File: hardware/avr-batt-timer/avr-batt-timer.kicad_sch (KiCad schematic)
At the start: 6 parts, among them Q1 RFP30N06LE, U1 ATtiny5-TS

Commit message: Added most components.
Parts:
- removed Q1: RFP30N06LE, Package_TO_SOT_THT:TO-220-3_Horizontal_TabDown, symbol Timofei_Import:RFP30N06LE
- added J1: XT60PW-M, Connector_AMASS:AMASS_XT60PW-M_1x02_P7.20mm_Horizontal, symbol Timofei_Import:XT60PW-M
- added J2: XT60PW-F, Connector_AMASS:AMASS_XT60PW-F_1x02_P7.20mm_Horizontal, symbol Timofei_Import:XT60PW-F
- added MOSFET1: IRFZ44N_127, Package_TO_SOT_THT:TO-220-2_Horizontal_TabDown, symbol Timofei_Import:IRFZ44N_127
- added R4: ~ 10K, Resistor_SMD:R_0805_2012Metric_Pad1.20x1.40mm_HandSolder, symbol Device:R
- added U2: L78L05_SOT89, Package_TO_SOT_SMD:SOT-89-3, symbol Regulator_Linear:L78L05_SOT89
- R1: value 2M2 -> 10M
- R2: value 10M -> 5M
- R3: value > 10K -> ~ 250R
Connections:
- net +3V3: no longer U1.5 (VCC)
- net GND: now also J1.1, J1.3, J1.4, J2.3 (MH1), J2.4 (MH2), MOSFET1.3 (S), R4.2, U2.2 (GND)
- net at R3.1: now also MOSFET1.1 (G), R4.1
- net TPICLK: now reaches R3.2, U1.4 (PB2)
- new net +5V: U1.5 (VCC), U2.1 (OUT)
- new net LOAD: J2.1, MOSFET1.2 (D)
- new net VDD: J1.2, J2.2, U2.3 (IN)
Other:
- note added: "ADD BACK-EMF PROTECTION DIODE!!!"
- note added: "ADD LED!!!"
- note added: "ADD TPICLK!!!!!"
- moved on the sheet: R3

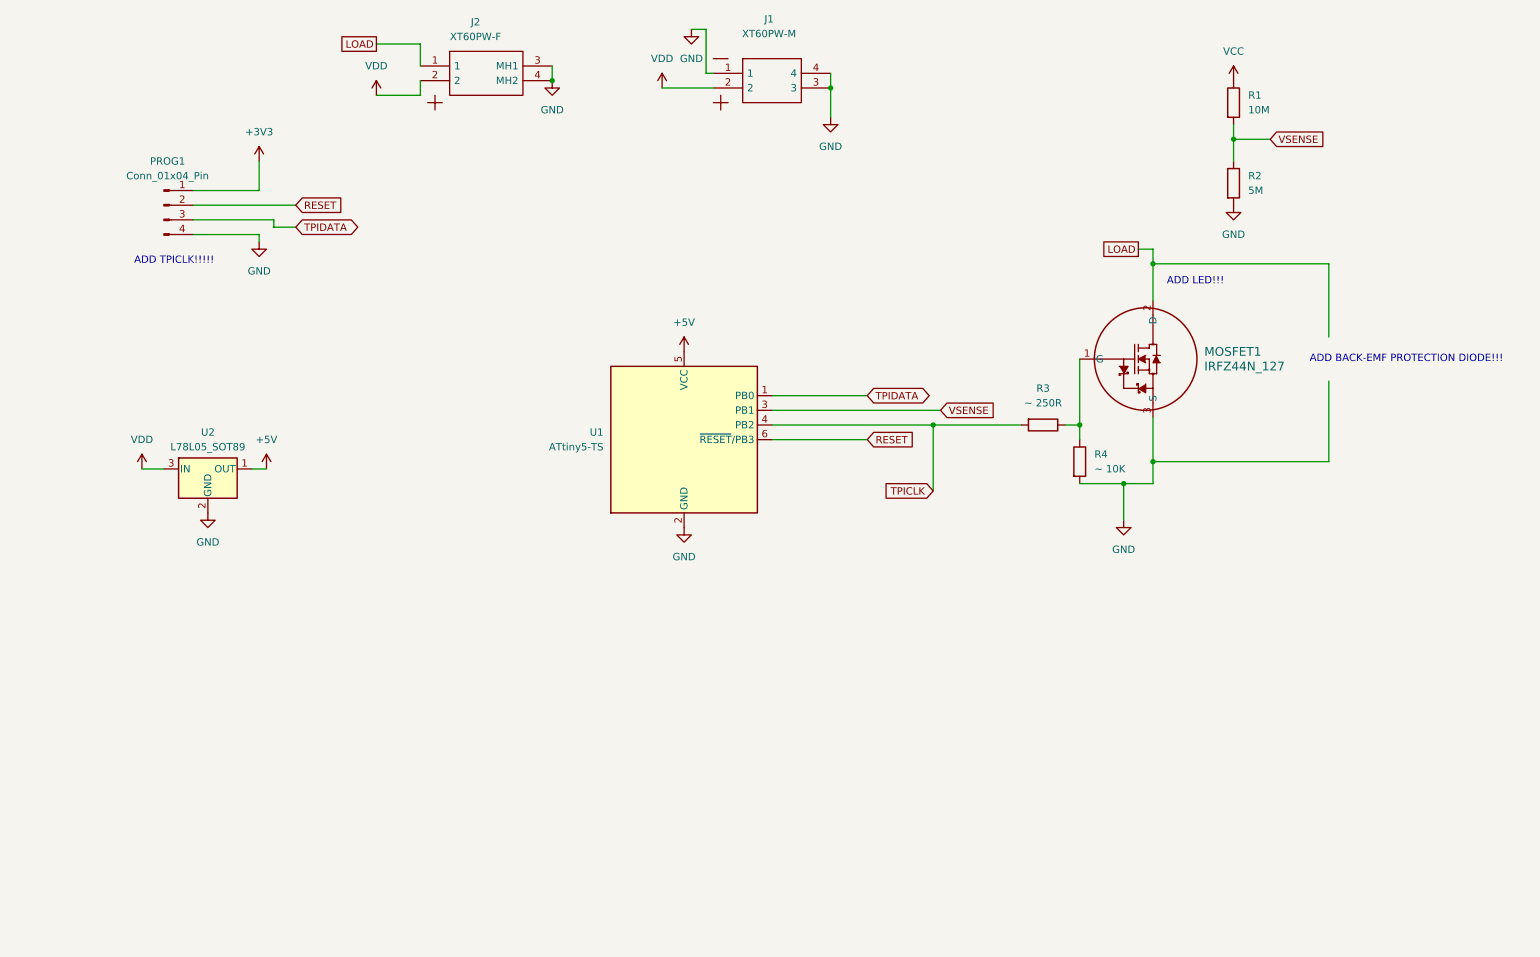
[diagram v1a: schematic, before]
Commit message: Added components. Initial PCB design.
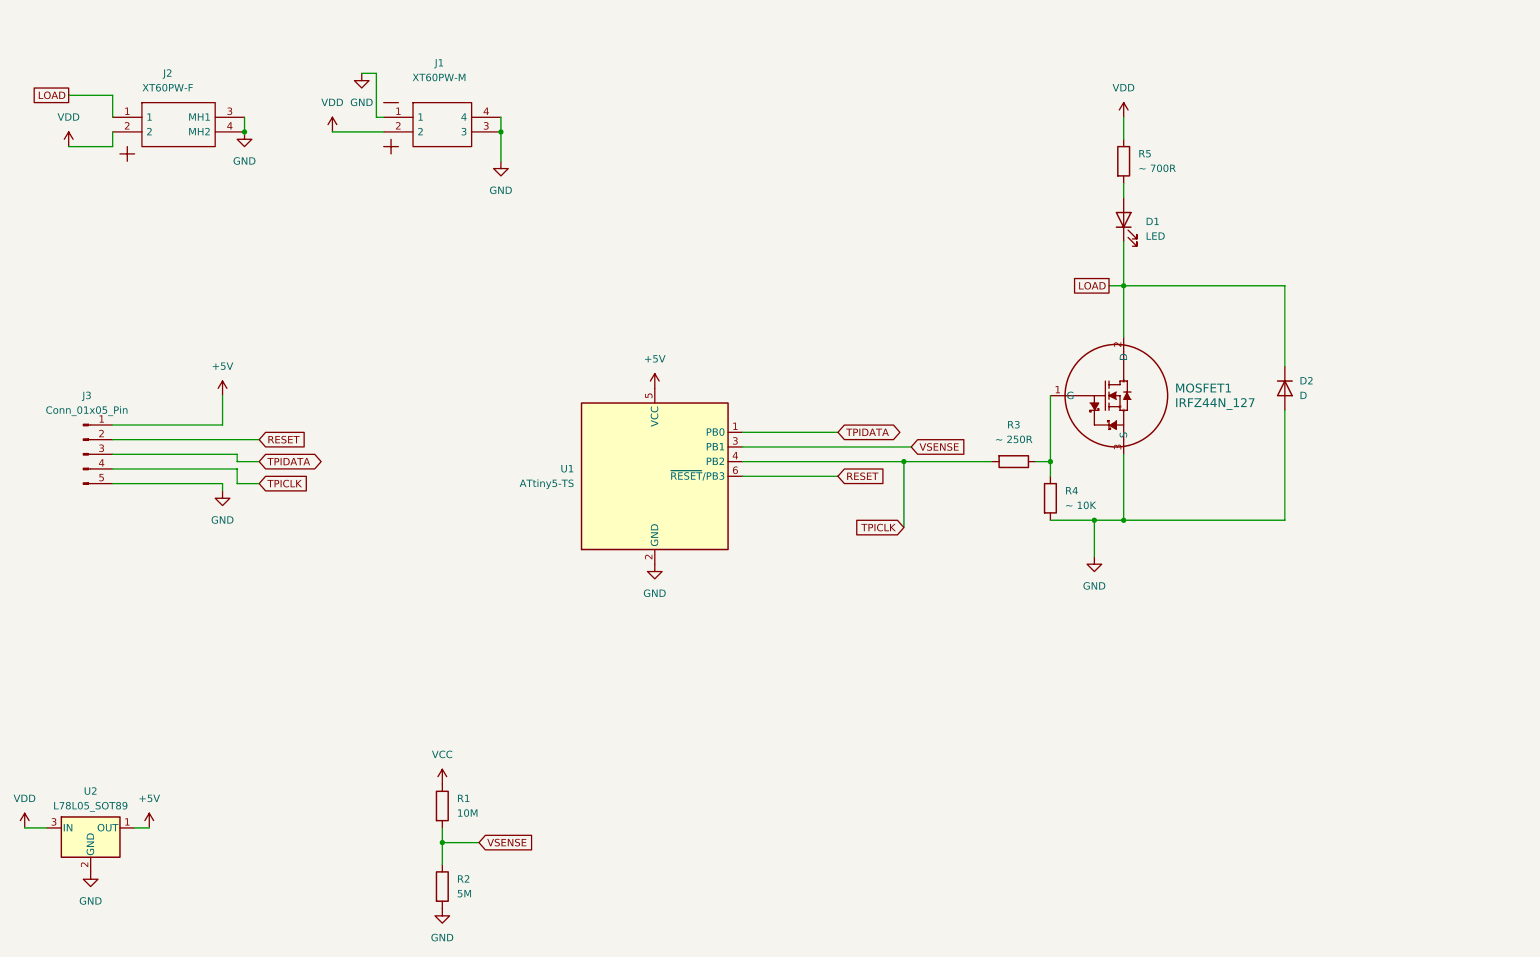
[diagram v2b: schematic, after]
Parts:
- removed PROG1: Conn_01x04_Pin, Connector_PinHeader_2.54mm:PinHeader_1x04_P2.54mm_Vertical, symbol Connector:Conn_01x04_Pin
- added D1: LED, LED_THT:LED_D3.0mm, symbol Device:LED
- added D2: D, Package_TO_SOT_THT:TO-220-2_Horizontal_TabDown, symbol Device:D
- added J3: Conn_01x05_Pin, Connector_PinHeader_2.54mm:PinHeader_1x05_P2.54mm_Vertical, symbol Connector:Conn_01x05_Pin
- added R5: ~ 700R, Resistor_SMD:R_0805_2012Metric_Pad1.20x1.40mm_HandSolder, symbol Device:R
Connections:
- net +5V: now also J3.1 (Pin_1)
- net GND: now also D2.2 (A), J3.5 (Pin_5)
- net LOAD: now also D1.1 (K), D2.1 (K)
- net RESET: now also J3.2 (Pin_2)
- net TPICLK: now also J3.4 (Pin_4)
- net TPIDATA: now also J3.3 (Pin_3)
- net VDD: now also R5.1
- new net: D1.2 (A), R5.2
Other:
- note removed: "ADD BACK-EMF PROTECTION DIODE!!!"
- note removed: "ADD LED!!!"
- note removed: "ADD TPICLK!!!!!"
- company: (none) -> Timofei Korostelev
- title: (none) -> avr-batt-timer
- moved on the sheet: J1, J2, MOSFET1, R1, R2, R3, R4, U1, U2

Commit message: +1
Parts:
- MOSFET1: footprint Package_TO_SOT_THT:TO-220-2_Horizontal_TabDown -> SOT78_TO220_NXP
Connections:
- net VCC is gone; now on net VDD: R1.1
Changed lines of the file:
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@@
+	(symbol
+		(lib_id "power:VDD")
+		(at 99.06 157.48 0)
+		(unit 1)
+		(exclude_from_sim no)
+		(in_bom yes)
+		(on_board yes)
+		(dnp no)
+		(fields_autoplaced yes)
+		(property "Reference" "#PWR06"
+			(at 99.06 161.29 0)
+			(effects
+				(font
+					(size 1.27 1.27)
+				)
+				(hide yes)
+			)
+		)
+		(property "Value" "VDD"
+			(at 99.06 152.4 0)
+			(effects
+				(font
+					(size 1.27 1.27)
+				)
+			)
+		)
+		(property "Footprint" ""
+			(at 99.06 157.48 0)
+			(effects
+				(font
+					(size 1.27 1.27)
+				)
+				(hide yes)
+			)
+		)
+		(property "Datasheet" ""
+			(at 99.06 157.48 0)
+			(effects
+				(font
+					(size 1.27 1.27)
+				)
+				(hide yes)
+			)
+		)
+		(property "Description" "Power symbol creates a global label with name \"VDD\""
+			(at 99.06 157.48 0)
+			(effects
+				(font
+					(size 1.27 1.27)
+				)
+				(hide yes)
+			)
+		)
+		(pin "1"
+		)
+		(instances
+			(project "avr-batt-timer"
+				(path "/3df09f8e-c59c-4ad6-a416-97010d9cd963"
+					(reference "#PWR06")
+					(unit 1)
+				)
+			)
+		)
+	)
 	(symbol
 		(lib_id "power:VDD")
@@
 	)
 	(symbol
-		(lib_id "power:VCC")
-		(at 99.06 157.48 0)
-		(unit 1)
-		(exclude_from_sim no)
-		(in_bom yes)
-		(on_board yes)
-		(dnp no)
-		(fields_autoplaced yes)
-		(property "Reference" "#PWR06"
-			(at 99.06 161.29 0)
-			(effects
-				(font
-					(size 1.27 1.27)
-				)
-				(hide yes)
-			)
-		)
-		(property "Value" "VCC"
-			(at 99.06 152.4 0)
-			(effects
-				(font
-					(size 1.27 1.27)
-				)
-			)
-		)
-		(property "Footprint" ""
-			(at 99.06 157.48 0)
-			(effects
-				(font
-					(size 1.27 1.27)
-				)
-				(hide yes)
-			)
-		)
-		(property "Datasheet" ""
-			(at 99.06 157.48 0)
-			(effects
-				(font
-					(size 1.27 1.27)
-				)
-				(hide yes)
-			)
-		)
-		(property "Description" "Power symbol creates a global label with name \"VCC\""
-			(at 99.06 157.48 0)
-			(effects
-				(font
-					(size 1.27 1.27)
-				)
-				(hide yes)
-			)
-		)
-		(pin "1"
-		)
-		(instances
-			(project ""
-				(path "/3df09f8e-c59c-4ad6-a416-97010d9cd963"
-					(reference "#PWR06")
-					(unit 1)
-				)
-			)
-		)
-	)
-	(symbol
 		(lib_id "MCU_Microchip_ATtiny:ATtiny5-TS")
 		(at 135.89 104.14 0)
@@
 			)
 		)
-		(property "Footprint" "Package_TO_SOT_THT:TO-220-2_Horizontal_TabDown"
+		(property "Footprint" "SOT78_TO220_NXP"
 			(at 198.12 83.058 0)
 			(effects

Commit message: +1
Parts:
- D2: value D -> D 15A
- MOSFET1: value IRFZ44N_127 -> IRFZ44N; footprint SOT78_TO220_NXP -> Package_TO_SOT_THT:TO-220-3_Horizontal_TabDown
- R3: value ~ 250R -> ~250R
- R4: value ~ 10K -> ~10K
- R5: value ~ 700R -> ~700R
- U1: value ATtiny5-TS -> ATtiny5
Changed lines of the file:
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@@
 			)
 		)
-		(property "Value" "~ 250R"
+		(property "Value" "~250R"
 			(at 198.12 97.79 90)
 			(effects
@@
 			)
 		)
-		(property "Value" "~ 700R"
+		(property "Value" "~700R"
 			(at 219.71 50.7999 0)
 			(effects
@@
 			)
 		)
-		(property "Value" "D"
+		(property "Value" "D 15A"
 			(at 247.65 90.1699 90)
 			(effects
@@
 			)
 		)
-		(property "Value" "~ 10K"
+		(property "Value" "~10K"
 			(at 207.01 109.2199 0)
 			(effects
@@
 			)
 		)
-		(property "Value" "ATtiny5-TS"
+		(property "Value" "ATtiny5"
 			(at 121.92 105.4099 0)
 			(effects
@@
 			)
 		)
-		(property "Value" "IRFZ44N_127"
+		(property "Value" "IRFZ44N"
 			(at 226.06 91.4399 0)
 			(effects
@@
 			)
 		)
-		(property "Footprint" "SOT78_TO220_NXP"
+		(property "Footprint" "Package_TO_SOT_THT:TO-220-3_Horizontal_TabDown"
 			(at 198.12 83.058 0)
 			(effects

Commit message: Fixed TPICLK pin connection. Replaced programming pins with holes.
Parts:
- removed J3: Conn_01x05_Pin, Connector_PinHeader_2.54mm:PinHeader_1x05_P2.54mm_Vertical, symbol Connector:Conn_01x05_Pin
- added TP1: +5V, TestPoint:TestPoint_Plated_Hole_D2.0mm, symbol Connector:TestPoint
- added TP2: RST, TestPoint:TestPoint_Plated_Hole_D2.0mm, symbol Connector:TestPoint
- added TP3: TDAT, TestPoint:TestPoint_Plated_Hole_D2.0mm, symbol Connector:TestPoint
- added TP4: TCLK, TestPoint:TestPoint_Plated_Hole_D2.0mm, symbol Connector:TestPoint
- added TP5: GND, TestPoint:TestPoint_Plated_Hole_D2.0mm, symbol Connector:TestPoint
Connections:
- net VSENSE is gone; now on net TPICLK: R1.2, R2.1, U1.3 (PB1)
- net +5V: now also TP1.1
- net GND: now also TP5.1
- net RESET: now also TP2.1
- net TPICLK: now also TP4.1; no longer R3.2, U1.4 (PB2)
- net TPIDATA: now also TP3.1
- new net: R3.2, U1.4 (PB2)
